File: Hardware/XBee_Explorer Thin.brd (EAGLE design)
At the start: 43.2 x 52.1 mm, 65 parts, among them J4 QWIIC_RIGHT_ANGLE, Q2 3.1A/30V/105mΩ, U1 FSUSB30MUX_MSOP10, U2 AP63203, U3 ESD Diode, U5 ESD Diode, U6 CP210X

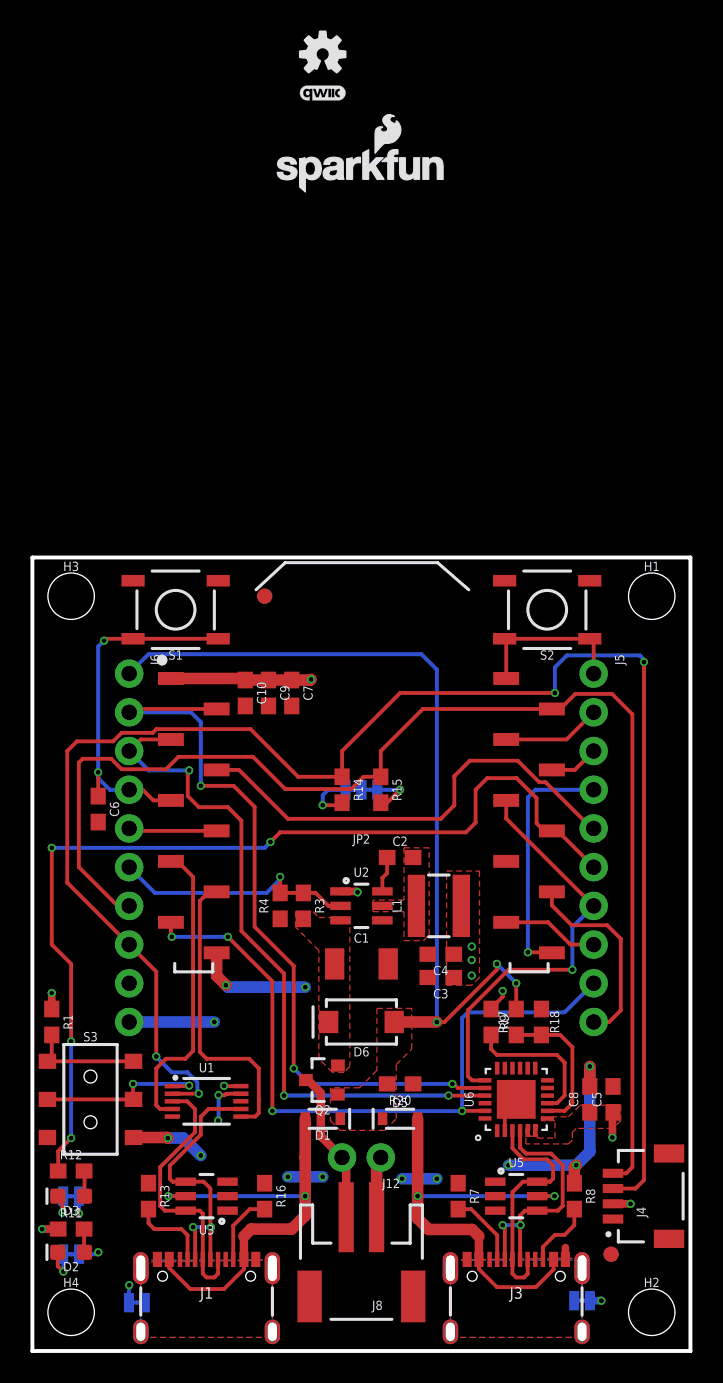
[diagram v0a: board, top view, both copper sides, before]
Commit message: Removes VIN from pin one one header and puts it at pin 10
* Shifts all other nets up one to accommodate VIN
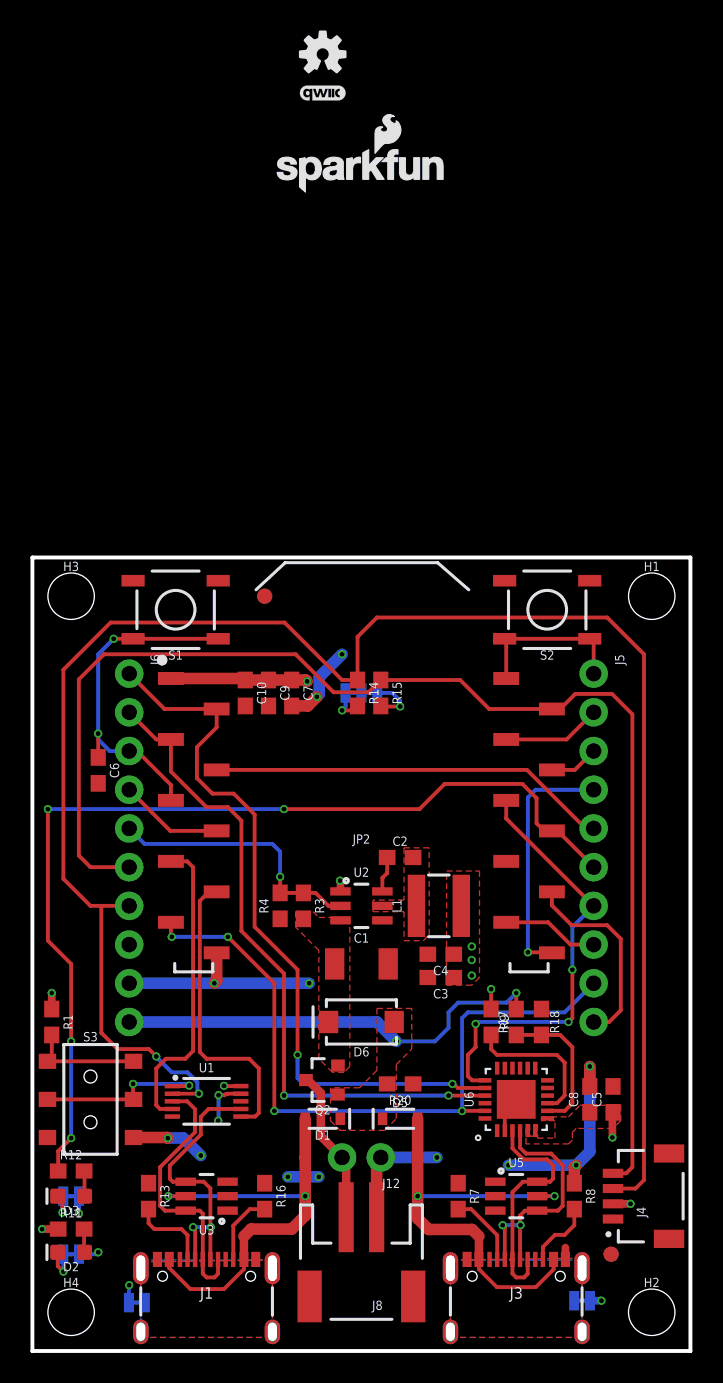
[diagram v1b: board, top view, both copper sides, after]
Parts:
- moved R14 6.43 mm to (21.3, 43.2)
- moved I2C_PU 6.35 mm to (21.6, 43.2)
- moved R15 6.35 mm to (22.9, 43.2)
- moved C6 2.54 mm to (4.32, 38.1)
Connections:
- net !RESET!: now also J6.3; no longer J6.4
- net 3.3V: now also J6.8; no longer J6.9
- net D1/SCL: now also J6.6; no longer J6.7
- net D10/RSSI_PWM: now also J6.4; no longer J6.5
- net D11/SDA: now also J6.7; no longer J6.8
- net D13/TXO: now also J6.1; no longer J6.2
- net D14/RXI: now also J6.2; no longer J6.3
- net EN: now also J6.5; no longer J6.6
- net GND: now also J6.9; no longer J6.10
- net VIN: now also J6.10; no longer J6.1
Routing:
- net VIN: track 56.3 -> 28.9 mm
- net D11/SDA: track 110.0 -> 119.4 mm, vias 4 -> 2
- net GND: track 51.3 -> 58.4 mm
- net D12/SPI_POCI: track 30.6 -> 26.3 mm
- net D13/TXO: track 50.4 -> 47.6 mm, vias 3 -> 2
- net D1/SCL: track 84.4 -> 86.5 mm
- net D14/RXI: track 45.8 -> 43.9 mm, vias 3 -> 2
- net EN: track 16.5 -> 17.7 mm
- net !RESET!: track 23.7 -> 22.5 mm
- net D10/RSSI_PWM: track 5.81 -> 6.86 mm
- net D6/!RTS!: track 27.6 -> 28.6 mm, vias 1 -> 3
- net N$11: track 3.65 -> 2.61 mm
- net 3.3V: track 17.9 -> 17.1 mm

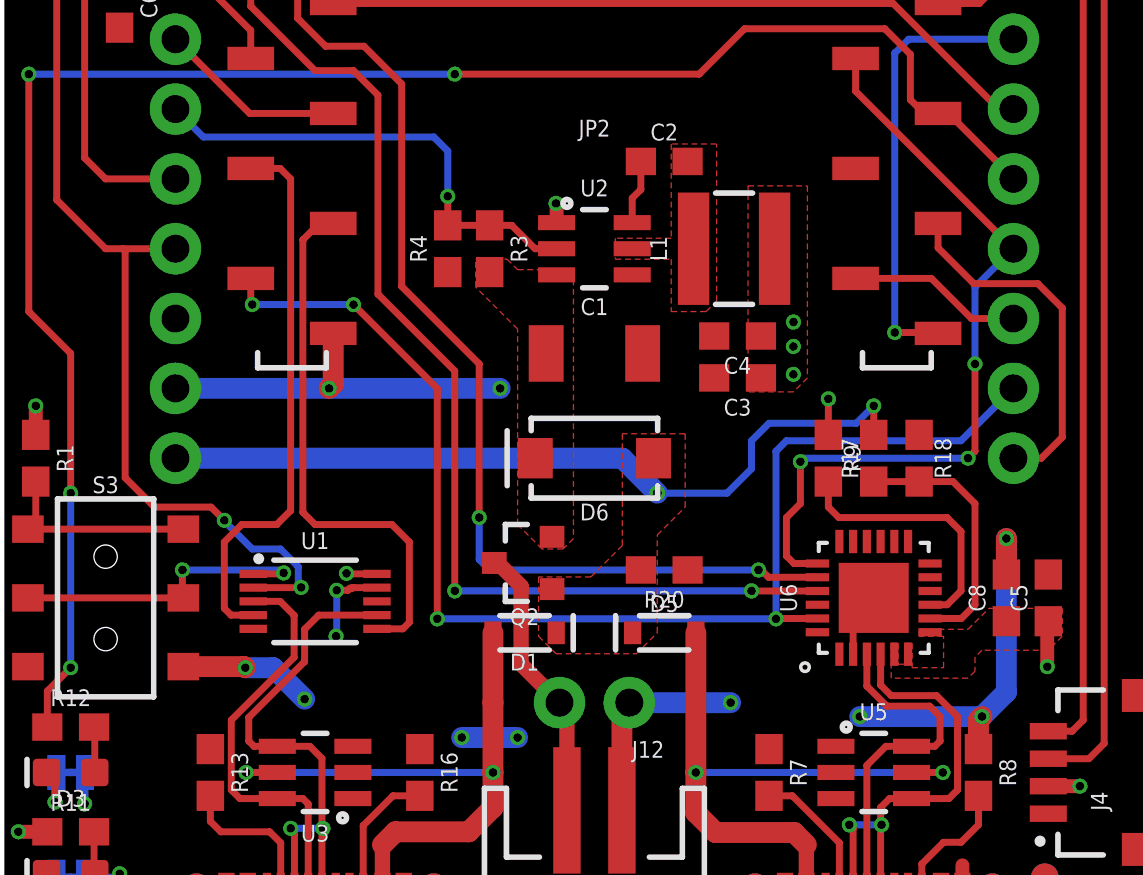
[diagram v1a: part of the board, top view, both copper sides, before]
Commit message: Updates some of the routing
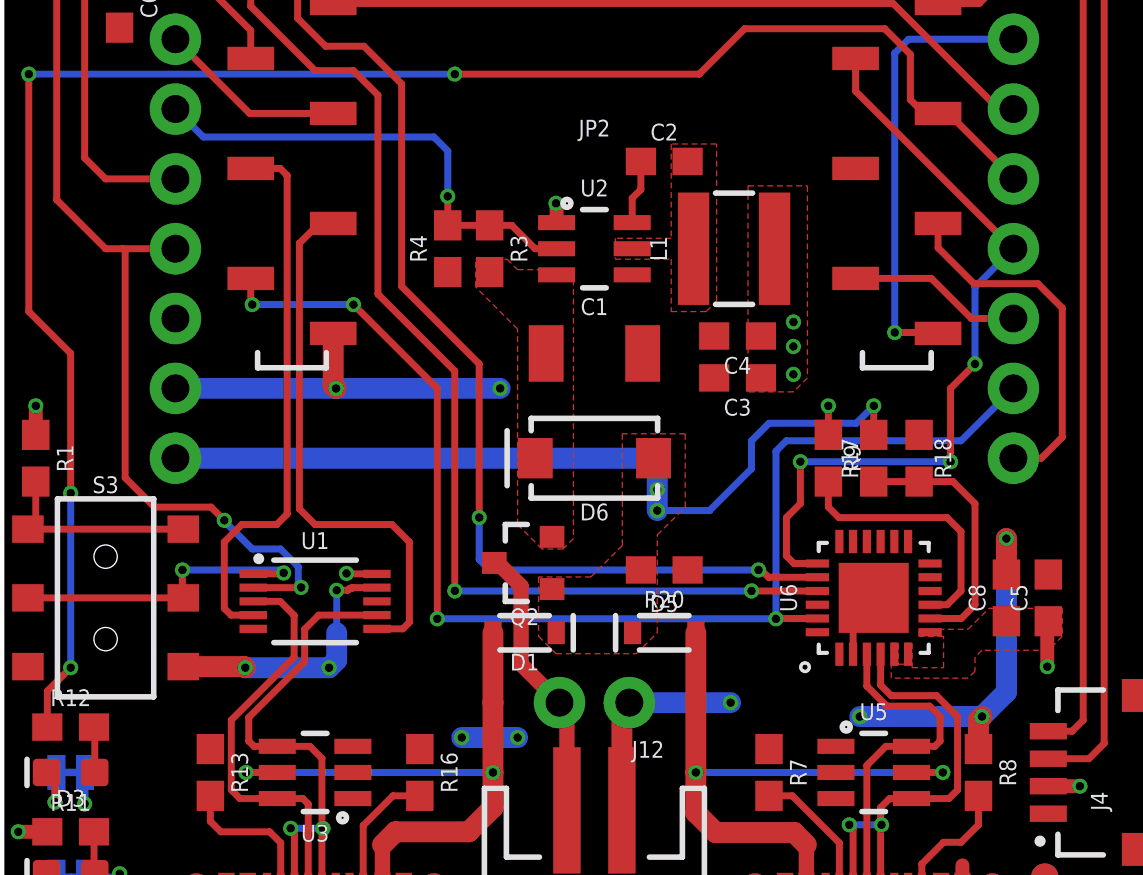
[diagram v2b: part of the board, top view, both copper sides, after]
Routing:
- net GND: track 58.4 -> 60.2 mm, vias 18 -> 17
- net VIN: track 28.9 -> 30.3 mm
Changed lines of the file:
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@@
 <wire x1="6.3373" y1="4.3053" x2="6.35" y2="4.318" width="0.254" layer="16"/>
 <via x="6.35" y="4.318" extent="1-16" drill="0.3048"/>
-<wire x1="12.09" y1="26.13" x2="12.09" y2="24.282" width="0.762" layer="1"/>
-<wire x1="12.09" y1="24.282" x2="11.938" y2="24.13" width="0.762" layer="1"/>
-<via x="11.938" y="24.13" extent="1-16" drill="0.3048"/>
-<wire x1="18.161" y1="24.13" x2="11.938" y2="24.13" width="0.762" layer="16"/>
+<wire x1="12.09" y1="26.13" x2="12.09" y2="24.232" width="0.762" layer="1"/>
+<wire x1="12.09" y1="24.232" x2="12.192" y2="24.13" width="0.762" layer="1"/>
+<via x="12.192" y="24.13" extent="1-16" drill="0.3048"/>
+<wire x1="18.161" y1="24.13" x2="12.192" y2="24.13" width="0.762" layer="16"/>
 <via x="18.161" y="24.13" extent="1-16" drill="0.3048"/>
 <wire x1="13.68" y1="16.883" x2="12.81134375" y2="16.883" width="0.254" layer="1"/>
@@
 <wire x1="8.85" y1="14.01" x2="8.89" y2="13.97" width="0.762" layer="1"/>
 <via x="8.89" y="13.97" extent="1-16" drill="0.3048"/>
-<wire x1="8.89" y1="13.97" x2="9.906" y2="13.97" width="0.762" layer="16"/>
-<wire x1="9.906" y1="13.97" x2="11.049" y2="12.827" width="0.762" layer="16"/>
-<via x="11.049" y="12.827" extent="1-16" drill="0.3048"/>
+<wire x1="8.89" y1="13.97" x2="11.938" y2="13.97" width="0.762" layer="16"/>
+<via x="11.938" y="13.97" extent="1-16" drill="0.3048"/>
 <wire x1="12.7" y1="16.8656" x2="12.621465625" y2="16.787065625" width="0.254" layer="1"/>
 <wire x1="12.621465625" y1="16.787065625" x2="12.215065625" y2="16.787065625" width="0.254" layer="1"/>
 <via x="12.215065625" y="16.787065625" extent="1-16" drill="0.3048"/>
-<wire x1="12.215065625" y1="16.787065625" x2="12.215065625" y2="15.136065625" width="0.254" layer="16"/>
-<wire x1="12.215065625" y1="15.136065625" x2="12.192" y2="15.113" width="0.254" layer="16"/>
-<via x="12.192" y="15.113" extent="1-16" drill="0.3048"/>
+<wire x1="12.215065625" y1="16.787065625" x2="12.215065625" y2="15.24" width="0.254" layer="16"/>
 <via x="16.764" y="11.43" extent="1-16" drill="0.3048"/>
+<wire x1="12.215065625" y1="15.24" x2="12.215065625" y2="15.136065625" width="0.254" layer="16"/>
 <wire x1="16.764" y1="11.43" x2="18.796" y2="11.43" width="0.762" layer="16"/>
 <via x="18.796" y="11.43" extent="1-16" drill="0.3048"/>
@@
 <wire x1="22.86" y1="12.7" x2="26.543" y2="12.7" width="0.762" layer="16"/>
 <contactref element="J6" pad="9"/>
-<wire x1="11.938" y1="24.13" x2="6.35" y2="24.13" width="0.762" layer="16"/>
+<wire x1="12.192" y1="24.13" x2="6.35" y2="24.13" width="0.762" layer="16"/>
 <wire x1="17.018" y1="42.33" x2="18.073" y2="42.33" width="0.762" layer="1"/>
 <wire x1="18.073" y1="42.33" x2="18.669" y2="42.926" width="0.762" layer="1"/>
@@
 <wire x1="18.8214" y1="43.10784375" x2="18.8214" y2="44.2214" width="0.762" layer="16"/>
 <wire x1="18.8214" y1="44.2214" x2="20.32" y2="45.72" width="0.762" layer="16"/>
+<wire x1="12.215065625" y1="15.24" x2="12.215065625" y2="14.247065625" width="0.762" layer="16"/>
+<wire x1="12.215065625" y1="14.247065625" x2="11.938" y2="13.97" width="0.762" layer="16"/>
 </signal>
 <signal name="3.3V">
@@
 <via x="28.829" y="24.638" extent="1-16" drill="0.3048"/>
 <contactref element="J6" pad="8"/>
-<via x="30.099" y="23.749" extent="1-16" drill="0.3048"/>
-<wire x1="30.099" y1="22.44" x2="30.099" y2="23.749" width="0.254" layer="1"/>
+<via x="30.099" y="23.495" extent="1-16" drill="0.3048"/>
+<wire x1="30.099" y1="22.44" x2="30.099" y2="23.495" width="0.254" layer="1"/>
 </signal>
 <signal name="V_USB">
@@
 <wire x1="29.083" y1="19.939" x2="29.083" y2="21.463" width="0.254" layer="1"/>
 <via x="29.083" y="21.463" extent="1-16" drill="0.3048"/>
-<wire x1="29.083" y1="21.463" x2="29.21" y2="21.59" width="0.254" layer="16"/>
-<wire x1="29.21" y1="21.59" x2="35.179" y2="21.59" width="0.254" layer="16"/>
-<via x="35.179" y="21.59" extent="1-16" drill="0.3048"/>
-<wire x1="35.179" y1="21.59" x2="35.433" y2="21.844" width="0.254" layer="1"/>
-<wire x1="35.433" y1="21.844" x2="35.433" y2="25.019" width="0.254" layer="1"/>
+<wire x1="29.083" y1="21.463" x2="34.544" y2="21.463" width="0.254" layer="16"/>
+<via x="34.544" y="21.463" extent="1-16" drill="0.3048"/>
+<wire x1="34.544" y1="24.13" x2="35.433" y2="25.019" width="0.254" layer="1"/>
+<wire x1="34.544" y1="24.13" x2="34.544" y2="21.463" width="0.254" layer="1"/>
 <wire x1="28.575" y1="19.431" x2="29.083" y2="19.939" width="0.254" layer="1"/>
 </signal>
@@
 <wire x1="8.128" y1="16.129" x2="8.128" y2="18.542" width="0.254" layer="1"/>
 <wire x1="9.78" y1="32.13" x2="9.779" y2="32.131" width="0.254" layer="1"/>
-<wire x1="9.526" y1="32.13" x2="9.78" y2="32.13" width="0.254" layer="1"/>
 <wire x1="8.763" y1="19.177" x2="10.033" y2="19.177" width="0.254" layer="1"/>
-<wire x1="10.033" y1="19.177" x2="10.541" y2="19.685" width="0.254" layer="1"/>
+<wire x1="10.033" y1="19.177" x2="10.414" y2="19.558" width="0.254" layer="1"/>
 <wire x1="8.128" y1="18.542" x2="8.763" y2="19.177" width="0.254" layer="1"/>
-<wire x1="10.541" y1="19.685" x2="10.541" y2="31.75" width="0.254" layer="1"/>
-<wire x1="9.09" y1="32.13" x2="9.526" y2="32.13" width="0.254" layer="1"/>
+<wire x1="10.414" y1="19.558" x2="10.414" y2="31.877" width="0.254" layer="1"/>
+<wire x1="9.09" y1="32.13" x2="9.78" y2="32.13" width="0.254" layer="1"/>
 <wire x1="9.78" y1="32.13" x2="10.161" y2="32.13" width="0.254" layer="1"/>
-<wire x1="10.161" y1="32.13" x2="10.541" y2="31.75" width="0.254" layer="1"/>
+<wire x1="10.161" y1="32.13" x2="10.414" y2="31.877" width="0.254" layer="1"/>
 </signal>
 <signal name="XBEE_D-">
@@
 <wire x1="14.224" y1="19.177" x2="11.43" y2="19.177" width="0.254" layer="1"/>
 <wire x1="11.582" y1="30.13" x2="12.09" y2="30.13" width="0.254" layer="1"/>
-<wire x1="11.582" y1="30.13" x2="10.986" y2="29.534" width="0.254" layer="1"/>
+<wire x1="11.582" y1="30.13" x2="10.859" y2="29.407" width="0.254" layer="1"/>
 <wire x1="14.859" y1="18.542" x2="14.224" y2="19.177" width="0.254" layer="1"/>
-<wire x1="10.986" y1="29.534" x2="10.986" y2="19.621" width="0.254" layer="1"/>
-<wire x1="10.986" y1="19.621" x2="11.43" y2="19.177" width="0.254" layer="1"/>
+<wire x1="10.859" y1="29.407" x2="10.859" y2="19.748" width="0.254" layer="1"/>
+<wire x1="10.859" y1="19.748" x2="11.43" y2="19.177" width="0.254" layer="1"/>
 </signal>
 <signal name="DIRECT_D+">
@@
 <via x="31.75" y="23.495" extent="1-16" drill="0.3048"/>
 <contactref element="J6" pad="10"/>
-<wire x1="6.35" y1="21.59" x2="22.606" y2="21.59" width="0.762" layer="16"/>
-<wire x1="22.606" y1="21.59" x2="23.876" y2="20.32" width="0.762" layer="16"/>
-<via x="23.876" y="20.32" extent="1-16" drill="0.3048"/>
+<wire x1="6.35" y1="21.59" x2="23.495" y2="21.59" width="0.762" layer="16"/>
+<wire x1="23.876" y1="21.209" x2="23.876" y2="19.685" width="0.762" layer="16"/>
+<wire x1="23.876" y1="21.209" x2="23.495" y2="21.59" width="0.762" layer="16"/>
+<via x="23.876" y="19.685" extent="1-16" drill="0.3048"/>
 <wire x1="31.115" y1="22.86" x2="31.75" y2="23.495" width="0.254" layer="16"/>
-<via x="23.876" y="20.32" extent="1-16" drill="0.3048"/>
-<wire x1="23.876" y1="20.32" x2="26.416" y2="20.32" width="0.254" layer="16"/>
+<wire x1="23.876" y1="19.685" x2="25.781" y2="19.685" width="0.254" layer="16"/>
 <wire x1="27.305" y1="21.209" x2="27.305" y2="22.225" width="0.254" layer="16"/>
 <wire x1="27.305" y1="22.225" x2="27.94" y2="22.86" width="0.254" layer="16"/>
 <wire x1="27.94" y1="22.86" x2="31.115" y2="22.86" width="0.254" layer="16"/>
-<wire x1="26.416" y1="20.32" x2="27.305" y2="21.209" width="0.254" layer="16"/>
+<wire x1="25.781" y1="19.685" x2="27.305" y2="21.209" width="0.254" layer="16"/>
+<via x="23.876" y="20.447" extent="1-16" drill="0.3048"/>
 </signal>
 <signal name="N$21">

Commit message: Adds additional vias for 3.3V output
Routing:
- net 3.3V: vias 11 -> 15
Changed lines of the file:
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@@
 <polygon width="0.127" layer="1" isolate="0.3048" thermals="no">
 <vertex x="27.178" y="24.003"/>
-<vertex x="27.178" y="31.496"/>
-<vertex x="29.337" y="31.496"/>
+<vertex x="27.178" y="33.401"/>
+<vertex x="29.337" y="33.401"/>
 <vertex x="29.337" y="24.511"/>
 <vertex x="28.829" y="24.003"/>
@@
 <via x="30.099" y="23.495" extent="1-16" drill="0.3048"/>
 <wire x1="30.099" y1="22.44" x2="30.099" y2="23.495" width="0.254" layer="1"/>
+<via x="27.813" y="32.131" extent="1-16" drill="0.3048"/>
+<via x="28.575" y="32.131" extent="1-16" drill="0.3048"/>
+<via x="27.813" y="32.893" extent="1-16" drill="0.3048"/>
+<via x="28.575" y="32.893" extent="1-16" drill="0.3048"/>
 </signal>
 <signal name="V_USB">

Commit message: Adds Measures
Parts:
- moved FRAME1 19.1 mm to (-6.35, -33.0)
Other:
- board text added: "Units in Inches"
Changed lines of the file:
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@@
 <layer number="45" name="Holes" color="7" fill="1" visible="yes" active="yes"/>
 <layer number="46" name="Milling" color="3" fill="1" visible="no" active="yes"/>
-<layer number="47" name="Measures" color="7" fill="1" visible="no" active="yes"/>
+<layer number="47" name="Measures" color="7" fill="1" visible="yes" active="yes"/>
 <layer number="48" name="Document" color="7" fill="1" visible="no" active="yes"/>
 <layer number="49" name="Reference" color="13" fill="1" visible="yes" active="yes"/>
@@
 <wire x1="43.18" y1="0" x2="43.18" y2="52.07" width="0.254" layer="20"/>
 <wire x1="43.18" y1="52.07" x2="0" y2="52.07" width="0.254" layer="20"/>
-<dimension x1="0" y1="41.91" x2="0" y2="0" x3="-15.24" y3="20.955" textsize="1.778" textratio="15" layer="47" unit="inch"/>
-<text x="20.32" y="-13.97" size="1.778" layer="51" font="vector">Elias Santistevan</text>
-<dimension x1="35.56" y1="41.91" x2="0" y2="41.91" x3="17.78" y3="54.61" textsize="1.778" layer="47" dtype="horizontal" unit="inch"/>
+<text x="20.32" y="-33.02" size="1.778" layer="51" font="vector">Elias Santistevan</text>
+<dimension x1="0" y1="52.07" x2="0" y2="0" x3="-12.7" y3="26.035" textsize="1.778" textratio="15" layer="47" unit="inch"/>
+<dimension x1="43.18" y1="52.07" x2="0" y2="52.07" x3="21.59" y3="60.96" textsize="1.778" textratio="15" layer="47" unit="inch"/>
+<dimension x1="21.59" y1="5.08" x2="0" y2="5.08" x3="10.795" y3="-15.24" textsize="1.778" textratio="15" layer="47" unit="inch"/>
+<dimension x1="11.43" y1="6.35" x2="0" y2="6.35" x3="5.715" y3="-10.16" textsize="1.778" textratio="15" layer="47" unit="inch"/>
+<dimension x1="2.54" y1="2.54" x2="0" y2="2.54" x3="1.27" y3="-5.08" textsize="1.778" textratio="15" layer="47" unit="inch"/>
+<dimension x1="31.75" y1="6.35" x2="43.18" y2="6.35" x3="37.465" y3="-10.16" textsize="1.778" textratio="15" layer="47" unit="inch"/>
+<dimension x1="0" y1="0" x2="31.75" y2="0" x3="15.875" y3="-21.59" textsize="1.778" textratio="15" layer="47" unit="inch"/>
+<dimension x1="2.54" y1="49.53" x2="2.54" y2="52.07" x3="-8.89" y3="50.8" textsize="1.778" textratio="15" layer="47" unit="inch"/>
+<dimension x1="21.59" y1="33.02" x2="21.59" y2="0" x3="-8.89" y3="16.51" textsize="1.778" textratio="15" layer="47" unit="inch"/>
+<dimension x1="6.35" y1="21.59" x2="6.35" y2="0" x3="-5.08" y3="10.795" textsize="1.778" textratio="15" layer="47" unit="inch"/>
+<text x="-21.59" y="-8.89" size="1.778" layer="47" font="vector" ratio="15">Units in Inches</text>
 </plain>
 <attributes>
@@
 </autorouter>
 <elements>
-<element name="FRAME1" library="SparkFun-Aesthetics" package="CREATIVE_COMMONS" value="FRAME-LEDGER" x="-6.35" y="-13.97" smashed="yes">
-<attribute name="DESIGNER" value="" x="-6.35" y="-13.97" size="1.778" layer="27" font="vector" ratio="15" display="off"/>
-<attribute name="REV" value="" x="-6.35" y="-13.97" size="1.778" layer="27" font="vector" ratio="15" display="off"/>
+<element name="FRAME1" library="SparkFun-Aesthetics" package="CREATIVE_COMMONS" value="FRAME-LEDGER" x="-6.35" y="-33.02" smashed="yes">
+<attribute name="DESIGNER" value="" x="-6.35" y="-33.02" size="1.778" layer="27" font="vector" ratio="15" display="off"/>
+<attribute name="REV" value="" x="-6.35" y="-33.02" size="1.778" layer="27" font="vector" ratio="15" display="off"/>
 </element>
 <element name="J8" library="SparkFun-Connectors" package="JST-2-SMD" value="" x="21.59" y="5.08" smashed="yes" rot="R180">
